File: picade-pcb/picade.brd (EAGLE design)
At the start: 70 x 60 mm, 59 parts

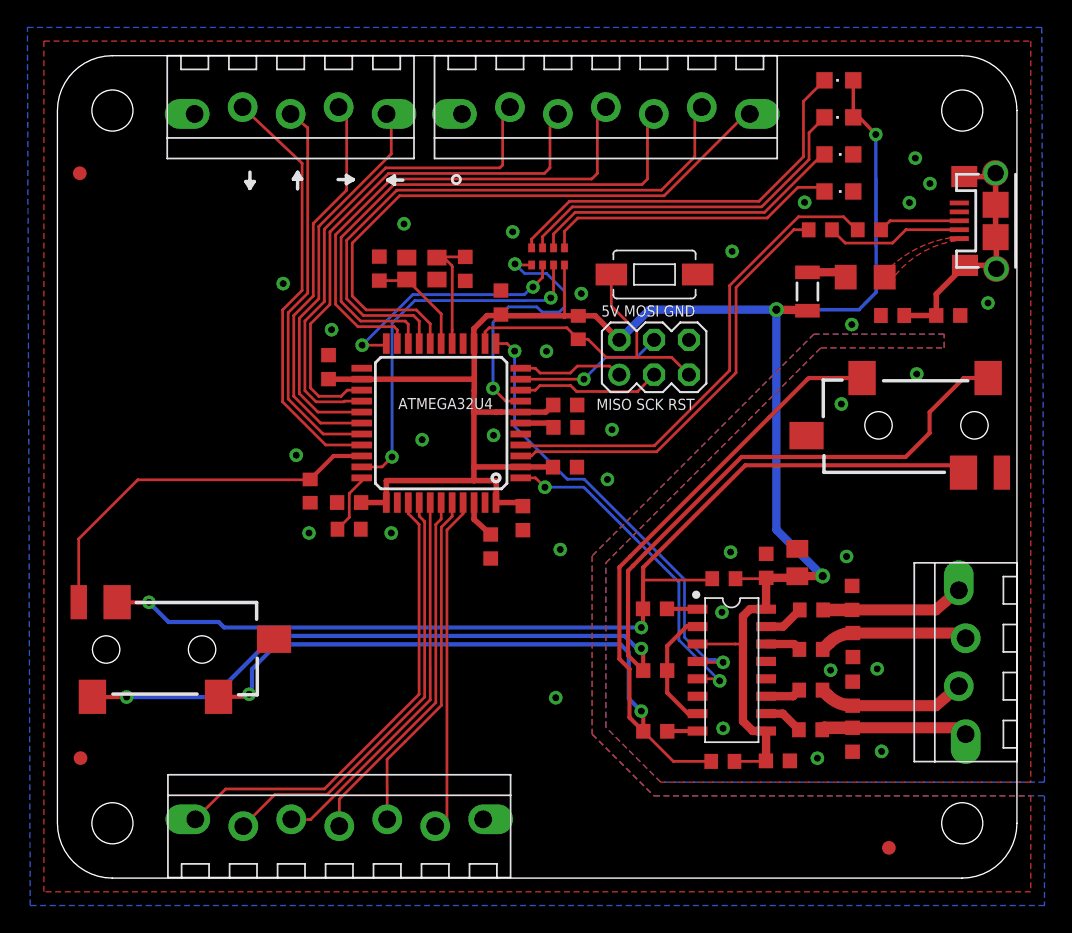
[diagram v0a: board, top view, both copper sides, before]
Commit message: Moved vias and stuff to avoid new silk
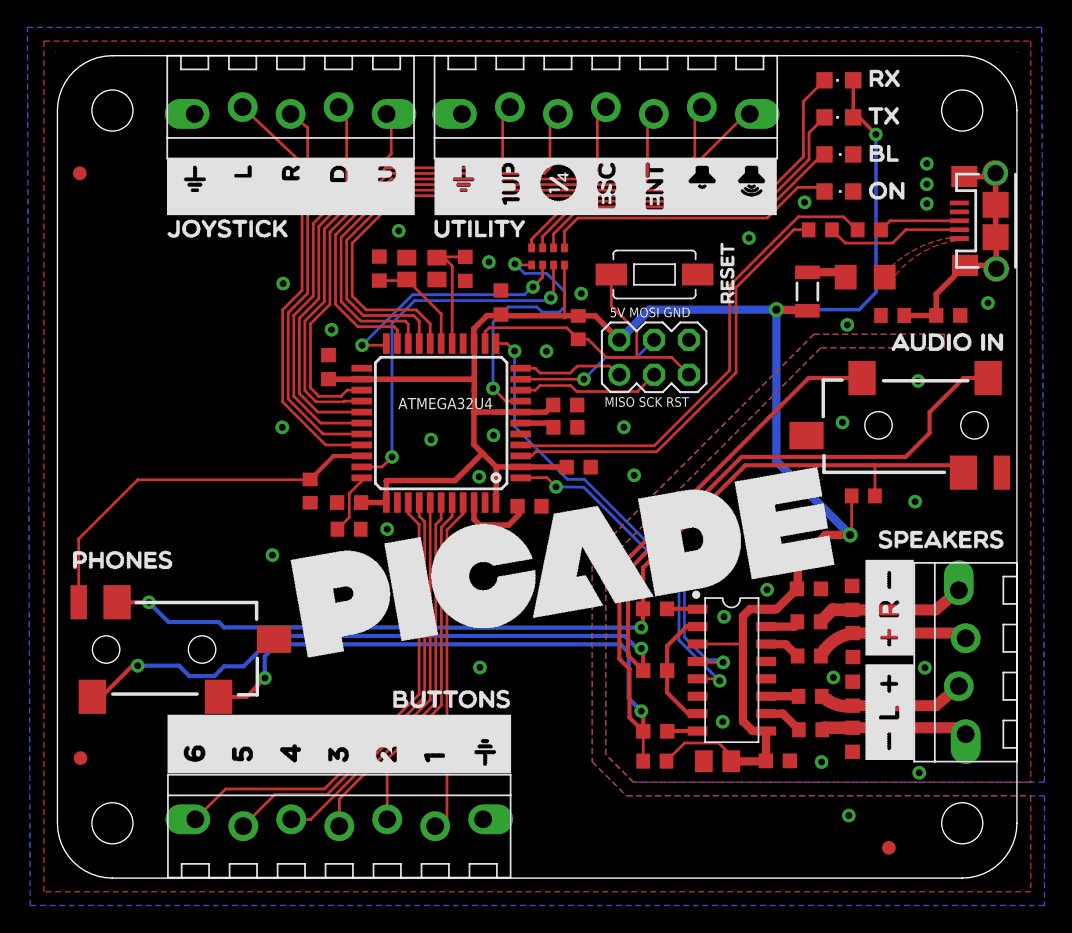
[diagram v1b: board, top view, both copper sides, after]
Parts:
- removed C10: 100nF, resistor:C0603K
- moved C16 15.6 mm to (48.1, 8.52), turned to 180 degrees
- moved R2 11.8 mm to (58.8, 27.9), turned to 180 degrees
- moved R3 4.96 mm to (43.6, 8.53)
- moved C8 4.08 mm to (34.4, 27.1), turned to 180 degrees
- moved C1 3.54 mm to (54.8, 21.1), turned to 0 degrees
- moved C4 1.00 mm to (38.0, 30.0)
- moved L1 0.88 mm to (54.8, 18.7)
- moved L2 0.50 mm to (54.8, 16.2)
- moved L4 0.46 mm to (54.9, 13.3)
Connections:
- net 5V: no longer C10.1
- net GND: no longer C10.2
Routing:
- net 5V: track 152.7 -> 158.2 mm
- net LINEINL+: track 80.9 -> 77.3 mm
- net LINEINR+: track 75.3 -> 72.4 mm
- net N$5: track 2.87 -> 5.61 mm
- net LINEIN-: track 84.7 -> 85.3 mm
- net SPEAKERR+: track 10.4 -> 11.0 mm
